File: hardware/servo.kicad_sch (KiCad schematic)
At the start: 12 parts, among them J11 AS5600, J15 IBT-2

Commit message: feat: MPN table merged into schematic fields; SES import script
Co-Authored-By: Claude Fable 5 <noreply@anthropic.com>
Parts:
- D10, D11, D8, D9: MPN (none) -> BAT54S,215
- J11: MPN (none) -> JST B4B-XH-A(LF)(SN)
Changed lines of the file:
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@@
     (property "Datasheet" "" (at 124.46 170.18 0)
+      (effects (font (size 1.27 1.27)) (hide yes)))
+    (property "MPN" "BAT54S,215" (at 124.46 170.18 0)
       (effects (font (size 1.27 1.27)) (hide yes)))
     (pin "1")
@@
       (effects (font (size 1.27 1.27)) (hide yes)))
     (property "Datasheet" "" (at 166.37 170.18 0)
+      (effects (font (size 1.27 1.27)) (hide yes)))
+    (property "MPN" "BAT54S,215" (at 166.37 170.18 0)
       (effects (font (size 1.27 1.27)) (hide yes)))
     (pin "1")
@@
     (property "Datasheet" "" (at 375.92 170.18 0)
       (effects (font (size 1.27 1.27)) (hide yes)))
+    (property "MPN" "BAT54S,215" (at 375.92 170.18 0)
+      (effects (font (size 1.27 1.27)) (hide yes)))
     (pin "1")
     (pin "2")
@@
       (effects (font (size 1.27 1.27)) (hide yes)))
     (property "Datasheet" "" (at 39.37 214.63 0)
+      (effects (font (size 1.27 1.27)) (hide yes)))
+    (property "MPN" "BAT54S,215" (at 39.37 214.63 0)
       (effects (font (size 1.27 1.27)) (hide yes)))
     (pin "1")
@@
     (property "Datasheet" "" (at 199.39 100.33 0)
       (effects (font (size 1.27 1.27)) (hide yes)))
+    (property "MPN" "JST B4B-XH-A(LF)(SN)" (at 199.39 100.33 0)
+      (effects (font (size 1.27 1.27)) (hide yes)))
     (pin "1")

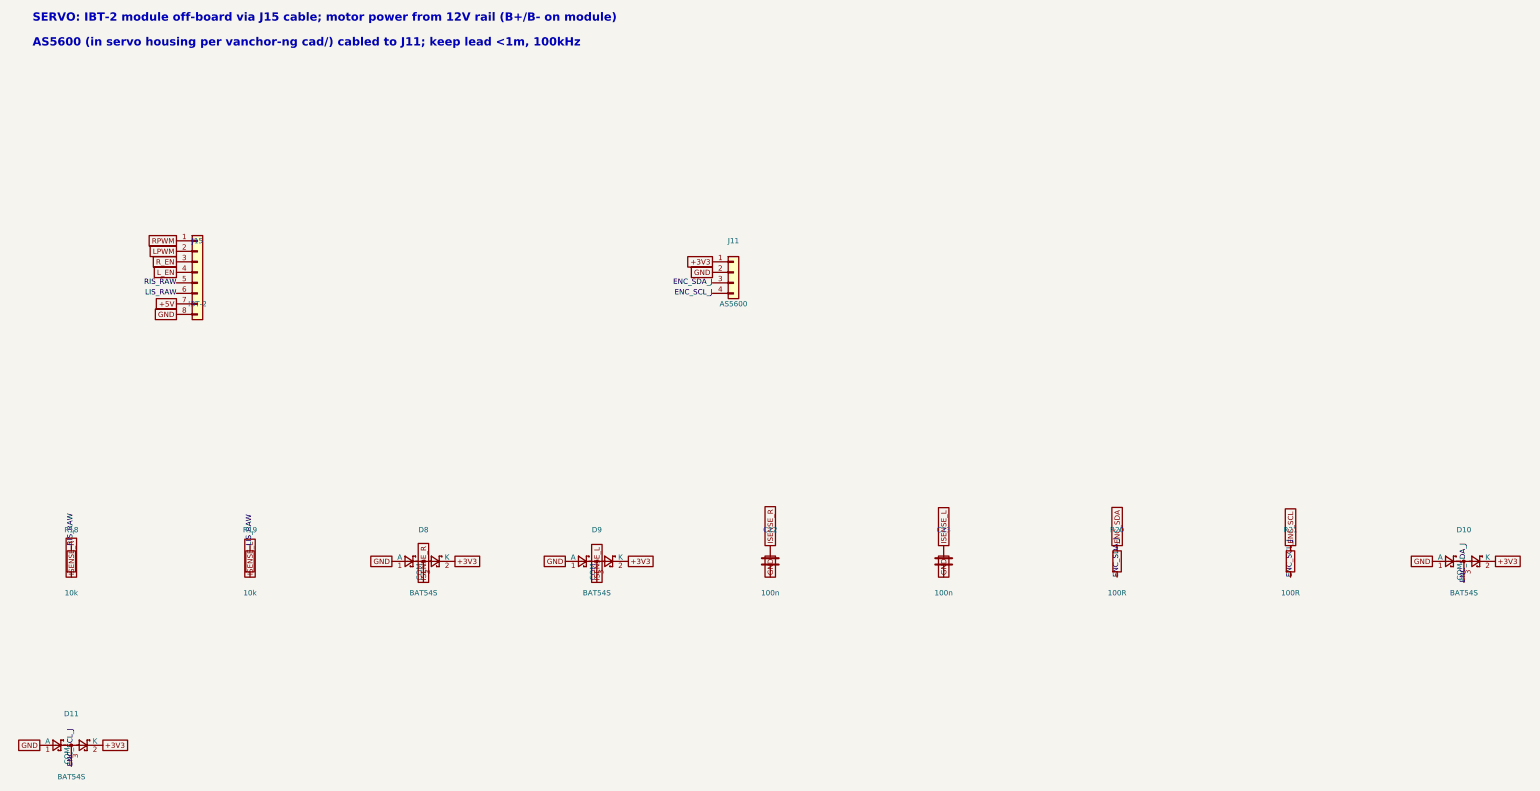
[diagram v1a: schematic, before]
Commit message: feat: on-board 800W H-bridge (HIP4082 + 8 FET, ACS758, M5 lugs) + BTN8982 servo bridge; 160x120 board, placement DRC-clean
Co-Authored-By: Claude Fable 5 <noreply@anthropic.com>
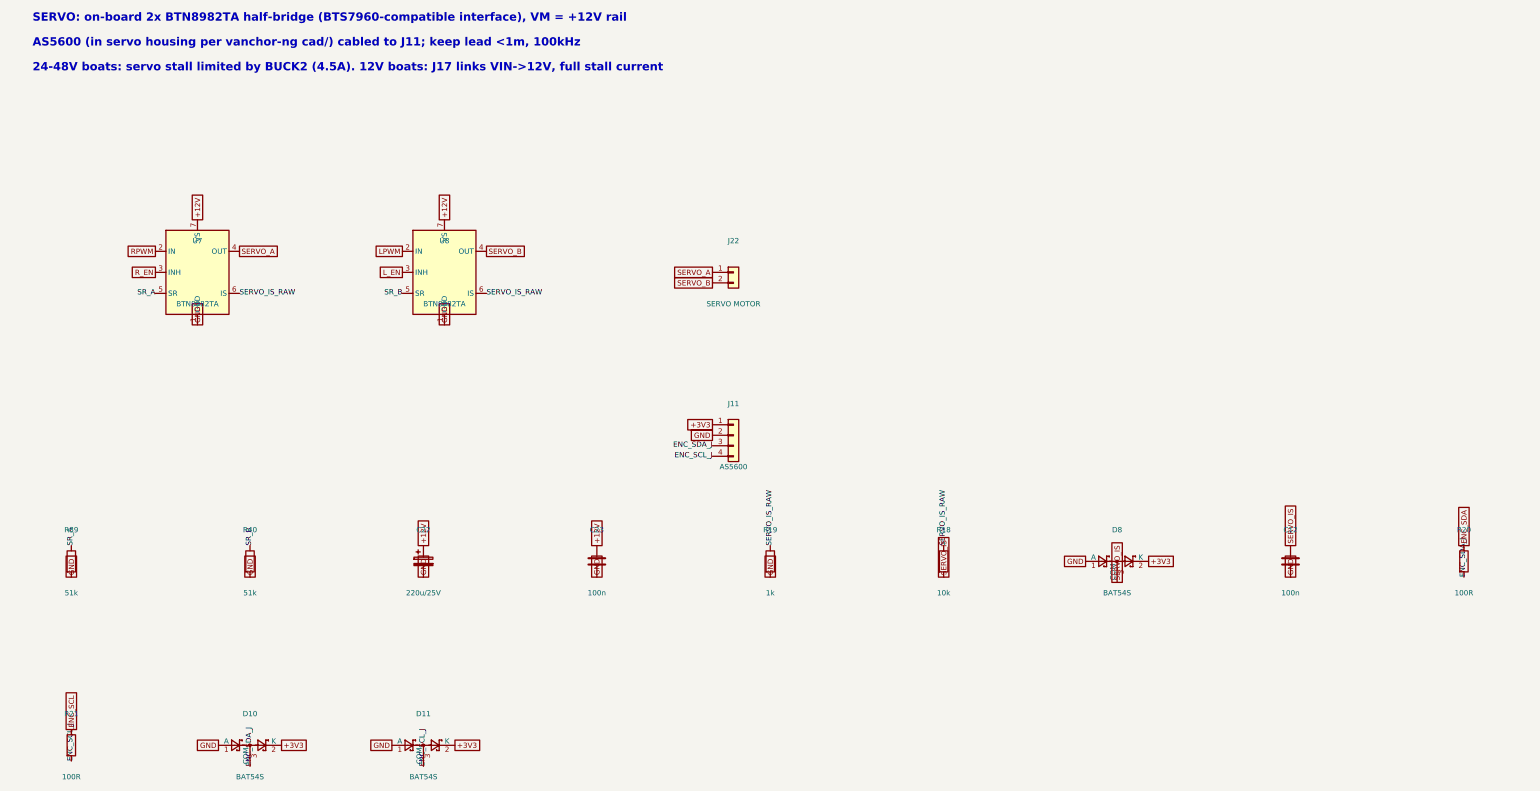
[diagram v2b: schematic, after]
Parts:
- removed C13: 100n, Capacitor_THT:C_Disc_D5.0mm_W2.5mm_P5.00mm, symbol Device:C
- removed D9: BAT54S, Package_TO_SOT_SMD:SOT-23, symbol Diode:BAT54S
- removed J15: IBT-2, Connector_PinHeader_2.54mm:PinHeader_1x08_P2.54mm_Vertical, symbol Connector_Generic:Conn_01x08
- added C22: 220u/25V, Capacitor_THT:CP_Radial_D8.0mm_P3.50mm, symbol Device:C_Polarized
- added C23: 100n, Capacitor_THT:C_Disc_D5.0mm_W2.5mm_P5.00mm, symbol Device:C
- added J22: SERVO MOTOR, TerminalBlock_CUI:TerminalBlock_CUI_TB007-508-02_1x02_P5.08mm_Horizontal, symbol Connector_Generic:Conn_01x02
- added R39, R40: 51k, Resistor_THT:R_Axial_DIN0207_L6.3mm_D2.5mm_P10.16mm_Horizontal, symbol Device:R
- added U7, U8: BTN8982TA, Package_TO_SOT_SMD:TO-263-7_TabPin4, symbol vanchor-helm:BTN8982TA
- R19: value 10k -> 1k
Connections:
- net ISENSE_L is gone; now on net GND: R19.2
- net RIS_RAW is gone; now on net SERVO_IS_RAW: R18.1
- net GND: now also C22.2, C23.2, R39.2, R40.2, U7.1 (GND), U8.1 (GND)
- net LPWM: now also U8.2 (IN)
- net L_EN: now also U8.3 (INH)
- net RPWM: now also U7.2 (IN)
- net R_EN: now also U7.3 (INH)
- net ISENSE_R renamed SERVO_IS
- net LIS_RAW renamed SERVO_IS_RAW
- net SERVO_IS_RAW: now also U7.6 (IS), U8.6 (IS)
- new net +12V: C22.1, C23.1, U7.7 (VS), U8.7 (VS)
- new net SERVO_A: J22.1 (Pin_1), U7.4 (OUT)
- new net SERVO_B: J22.2 (Pin_2), U8.4 (OUT)
- new net SR_A: R39.1, U7.5 (SR)
- new net SR_B: R40.1, U8.5 (SR)
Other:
- note added: "24-48V boats: servo stall limited by BUCK2 (4.5A). 12V boats: J17 links VIN->12V, full stall current"
- note added: "SERVO: on-board 2x BTN8982TA half-bridge (BTS7960-compatible interface), VM = +12V rail"
- note removed: "SERVO: IBT-2 module off-board via J15 cable; motor power from 12V rail (B+/B- on module)"
- moved on the sheet: C12, D10, D11, D8, J11, R18, R19, R20, R21

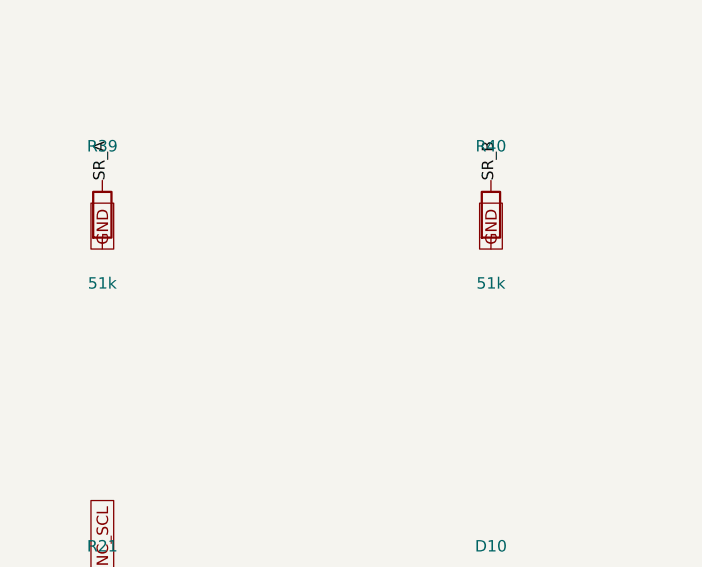
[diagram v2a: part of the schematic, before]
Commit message: cost pass 10 (schematic): remove on-board H-bridge, add J13 external-driver header (IBT-2 pinout); ERC 0, gate PASS
Co-Authored-By: Claude Fable 5 <noreply@anthropic.com>
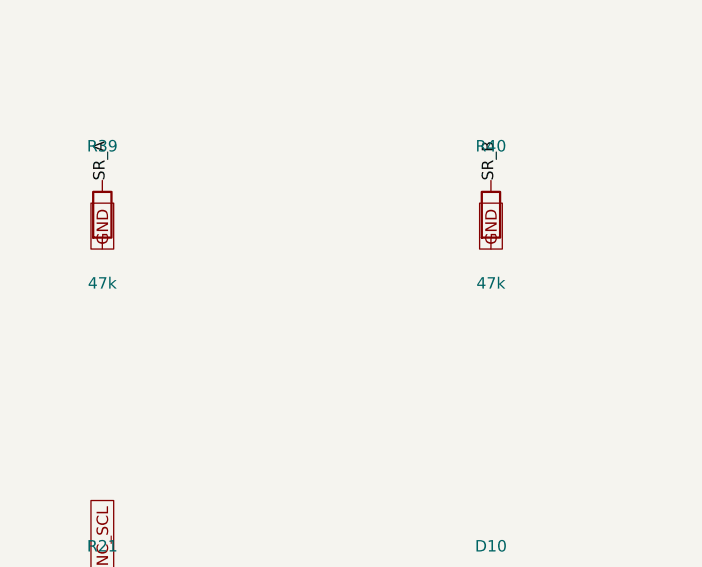
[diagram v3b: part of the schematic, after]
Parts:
- R39, R40: value 51k -> 47k
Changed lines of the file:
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@@
     (property "Reference" "R39" (at 39.37 162.56 0)
       (effects (font (size 1.27 1.27))))
-    (property "Value" "51k" (at 39.37 177.8 0)
+    (property "Value" "47k" (at 39.37 177.8 0)
       (effects (font (size 1.27 1.27))))
     (property "Footprint" "Resistor_THT:R_Axial_DIN0207_L6.3mm_D2.5mm_P10.16mm_Horizontal" (at 39.37 170.18 0)
@@
     (property "Reference" "R40" (at 82.55 162.56 0)
       (effects (font (size 1.27 1.27))))
-    (property "Value" "51k" (at 82.55 177.8 0)
+    (property "Value" "47k" (at 82.55 177.8 0)
       (effects (font (size 1.27 1.27))))
     (property "Footprint" "Resistor_THT:R_Axial_DIN0207_L6.3mm_D2.5mm_P10.16mm_Horizontal" (at 82.55 170.18 0)

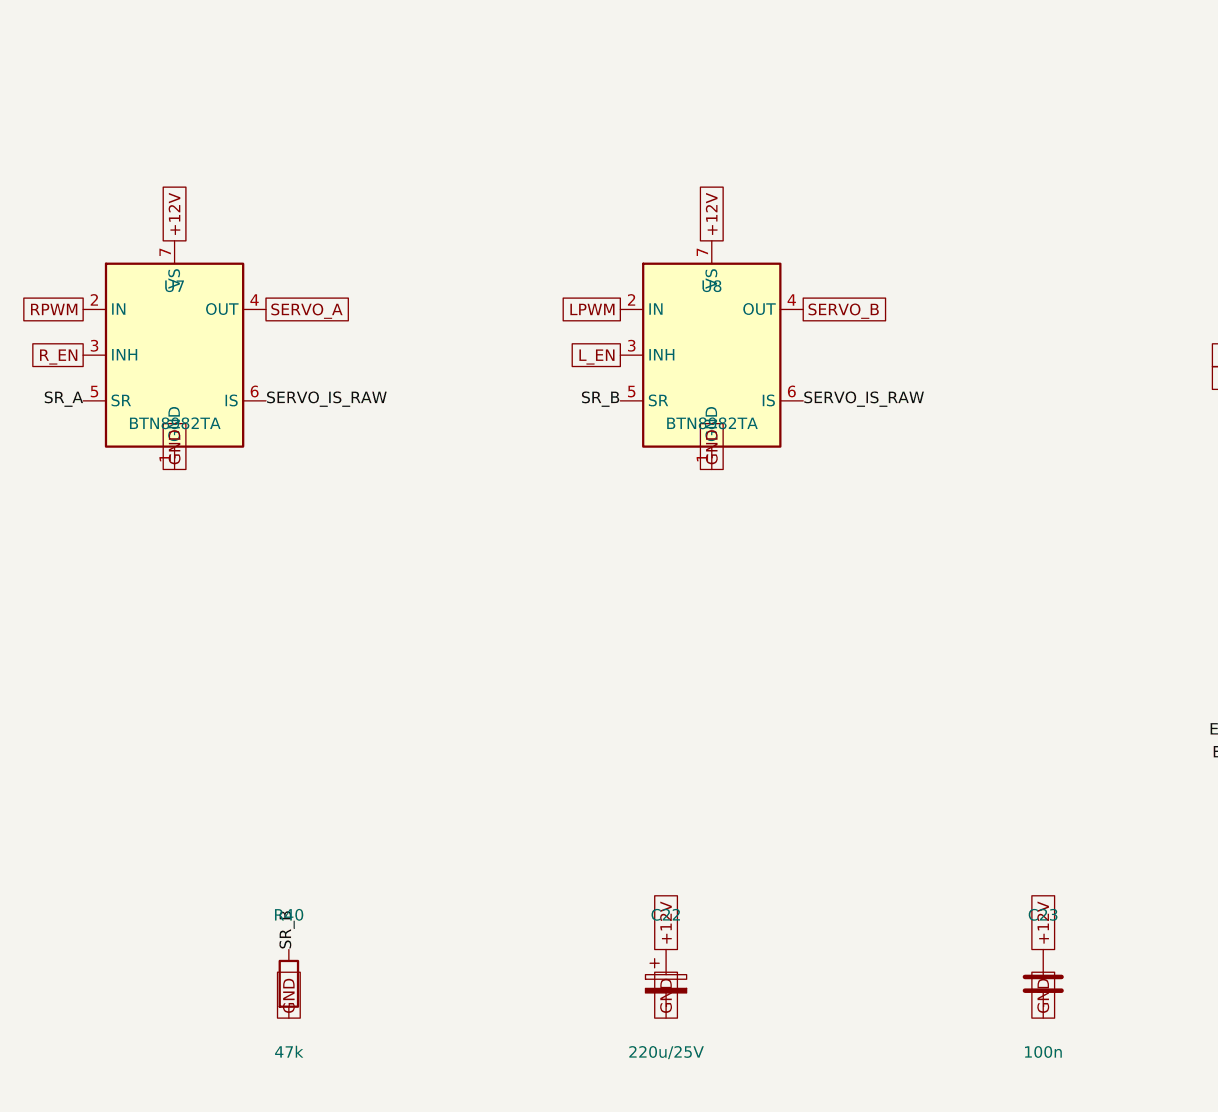
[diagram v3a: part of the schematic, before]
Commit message: feat: v3.1 12V-only — generic 5V buck module on J14, U5/U6/J17 removed, SMCJ18A TVS, servo direct on VIN; DRC clean
Co-Authored-By: Claude Fable 5 <noreply@anthropic.com>
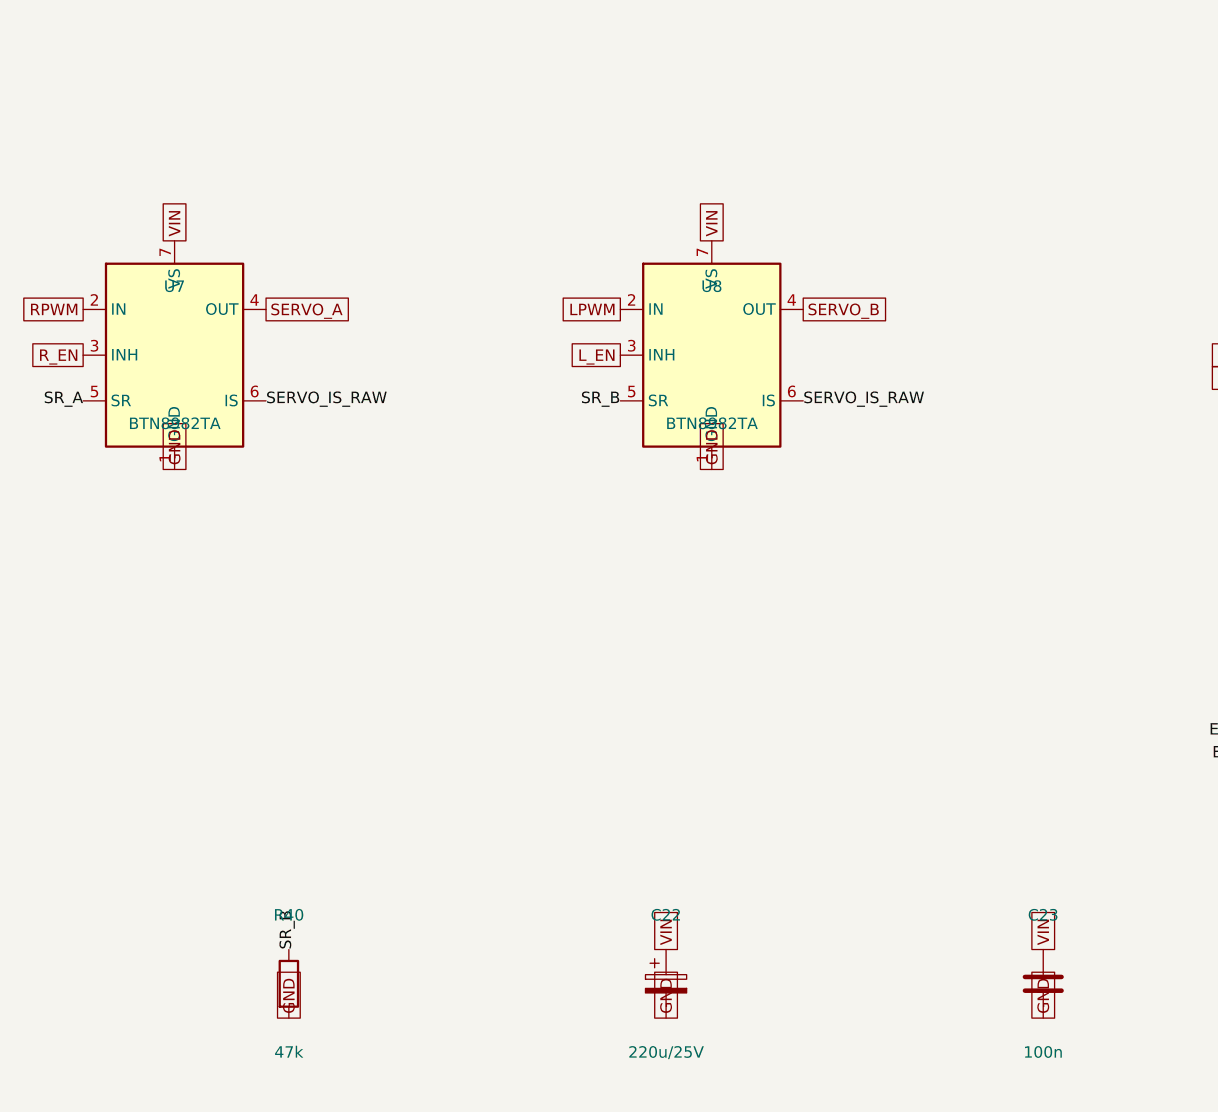
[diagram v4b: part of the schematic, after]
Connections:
- net +12V renamed VIN
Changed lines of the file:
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@@
     (effects (font (size 1.27 1.27)) (justify left))
   )
-  (global_label "+12V" (shape passive) (at 69.85 87.63 90.0) (fields_autoplaced yes)
+  (global_label "VIN" (shape passive) (at 69.85 87.63 90.0) (fields_autoplaced yes)
     (effects (font (size 1.27 1.27)) (justify left))
     (property "Intersheetrefs" "${INTERSHEET_REFS}" (at 69.85 87.63 0)
@@
     (effects (font (size 1.27 1.27)) (justify left))
   )
-  (global_label "+12V" (shape passive) (at 129.54 87.63 90.0) (fields_autoplaced yes)
+  (global_label "VIN" (shape passive) (at 129.54 87.63 90.0) (fields_autoplaced yes)
     (effects (font (size 1.27 1.27)) (justify left))
     (property "Intersheetrefs" "${INTERSHEET_REFS}" (at 129.54 87.63 0)
@@
       (effects (font (size 1.27 1.27)) (hide yes)))
   )
-  (global_label "+12V" (shape passive) (at 124.46 166.37 90.0) (fields_autoplaced yes)
+  (global_label "VIN" (shape passive) (at 124.46 166.37 90.0) (fields_autoplaced yes)
     (effects (font (size 1.27 1.27)) (justify left))
     (property "Intersheetrefs" "${INTERSHEET_REFS}" (at 124.46 166.37 0)
@@
       (effects (font (size 1.27 1.27)) (hide yes)))
   )
-  (global_label "+12V" (shape passive) (at 166.37 166.37 90.0) (fields_autoplaced yes)
+  (global_label "VIN" (shape passive) (at 166.37 166.37 90.0) (fields_autoplaced yes)
     (effects (font (size 1.27 1.27)) (justify left))
     (property "Intersheetrefs" "${INTERSHEET_REFS}" (at 166.37 166.37 0)
